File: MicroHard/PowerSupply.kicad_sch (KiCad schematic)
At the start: 40 parts, among them J1 USB_B_Micro, U1 TPS54325, U2 TPS54294

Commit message: VGA and Display layout
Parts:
- R8: value 68 -> 330
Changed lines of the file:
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@@
 			)
 		)
-		(property "Value" "68"
+		(property "Value" "330"
 			(at 240.284 133.604 0)
 			(effects

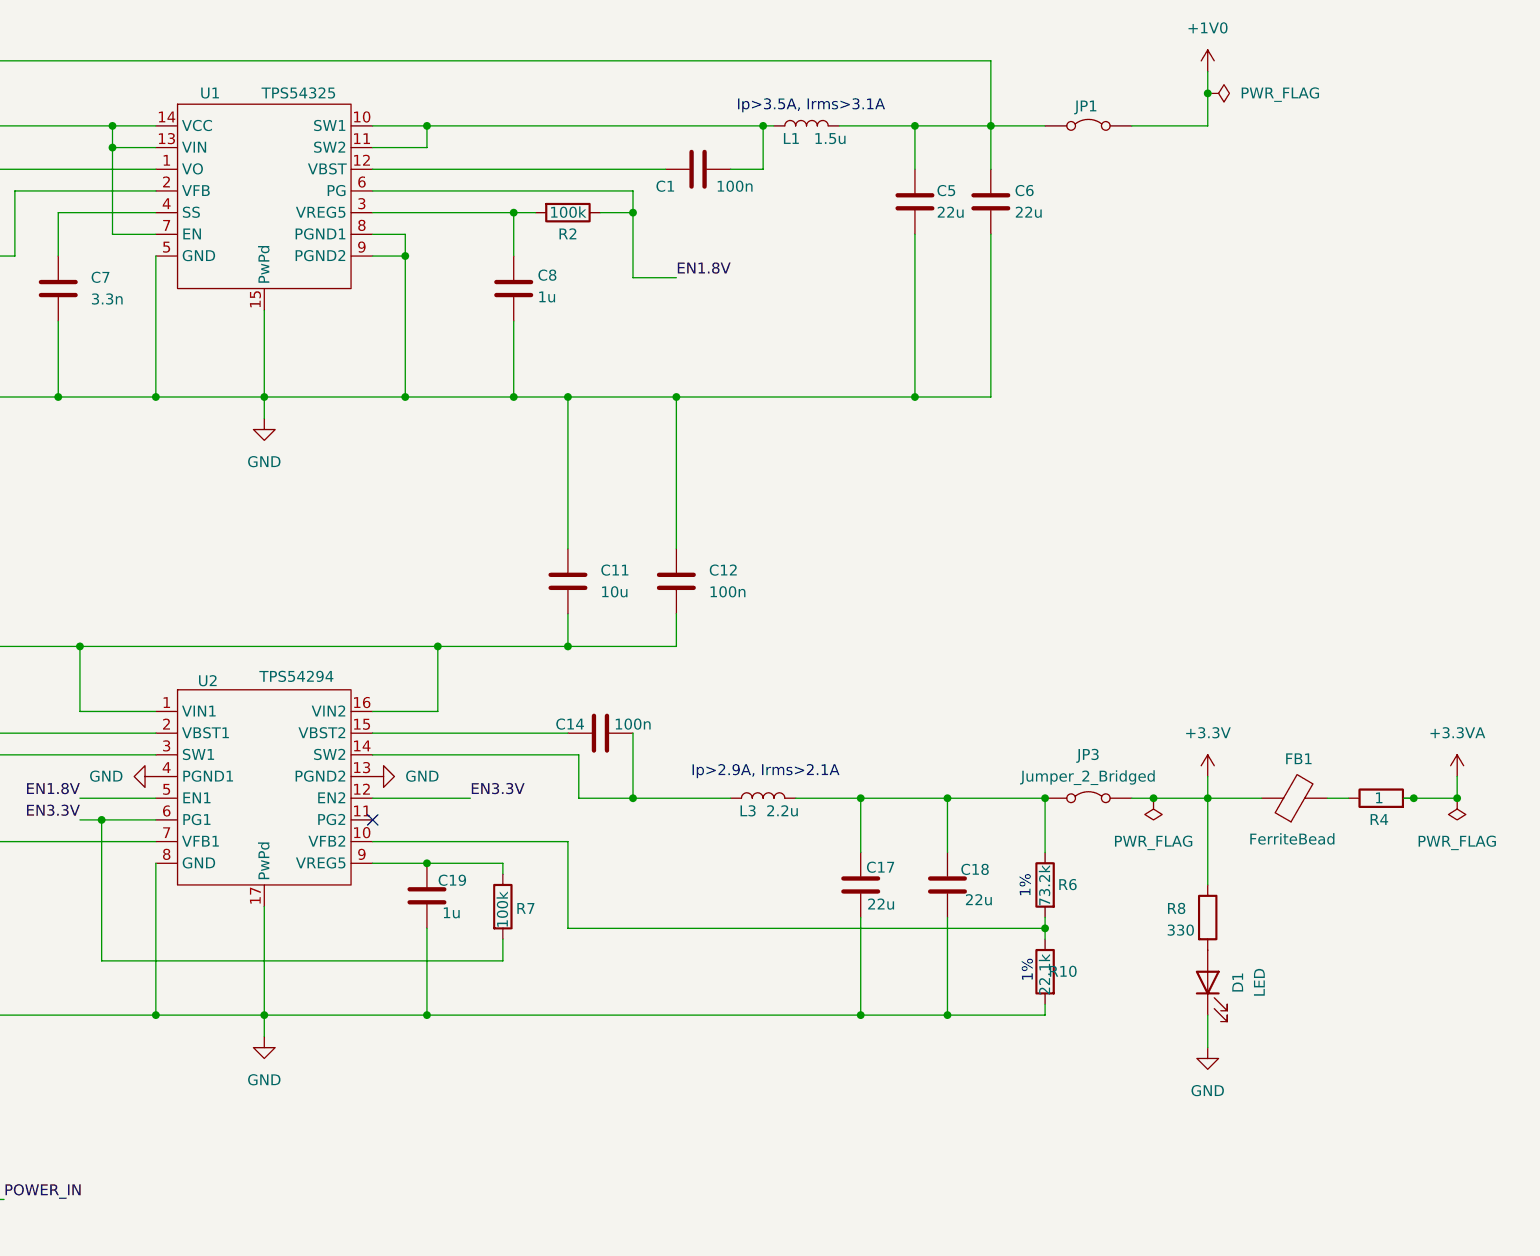
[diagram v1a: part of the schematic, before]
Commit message: Power supply layout
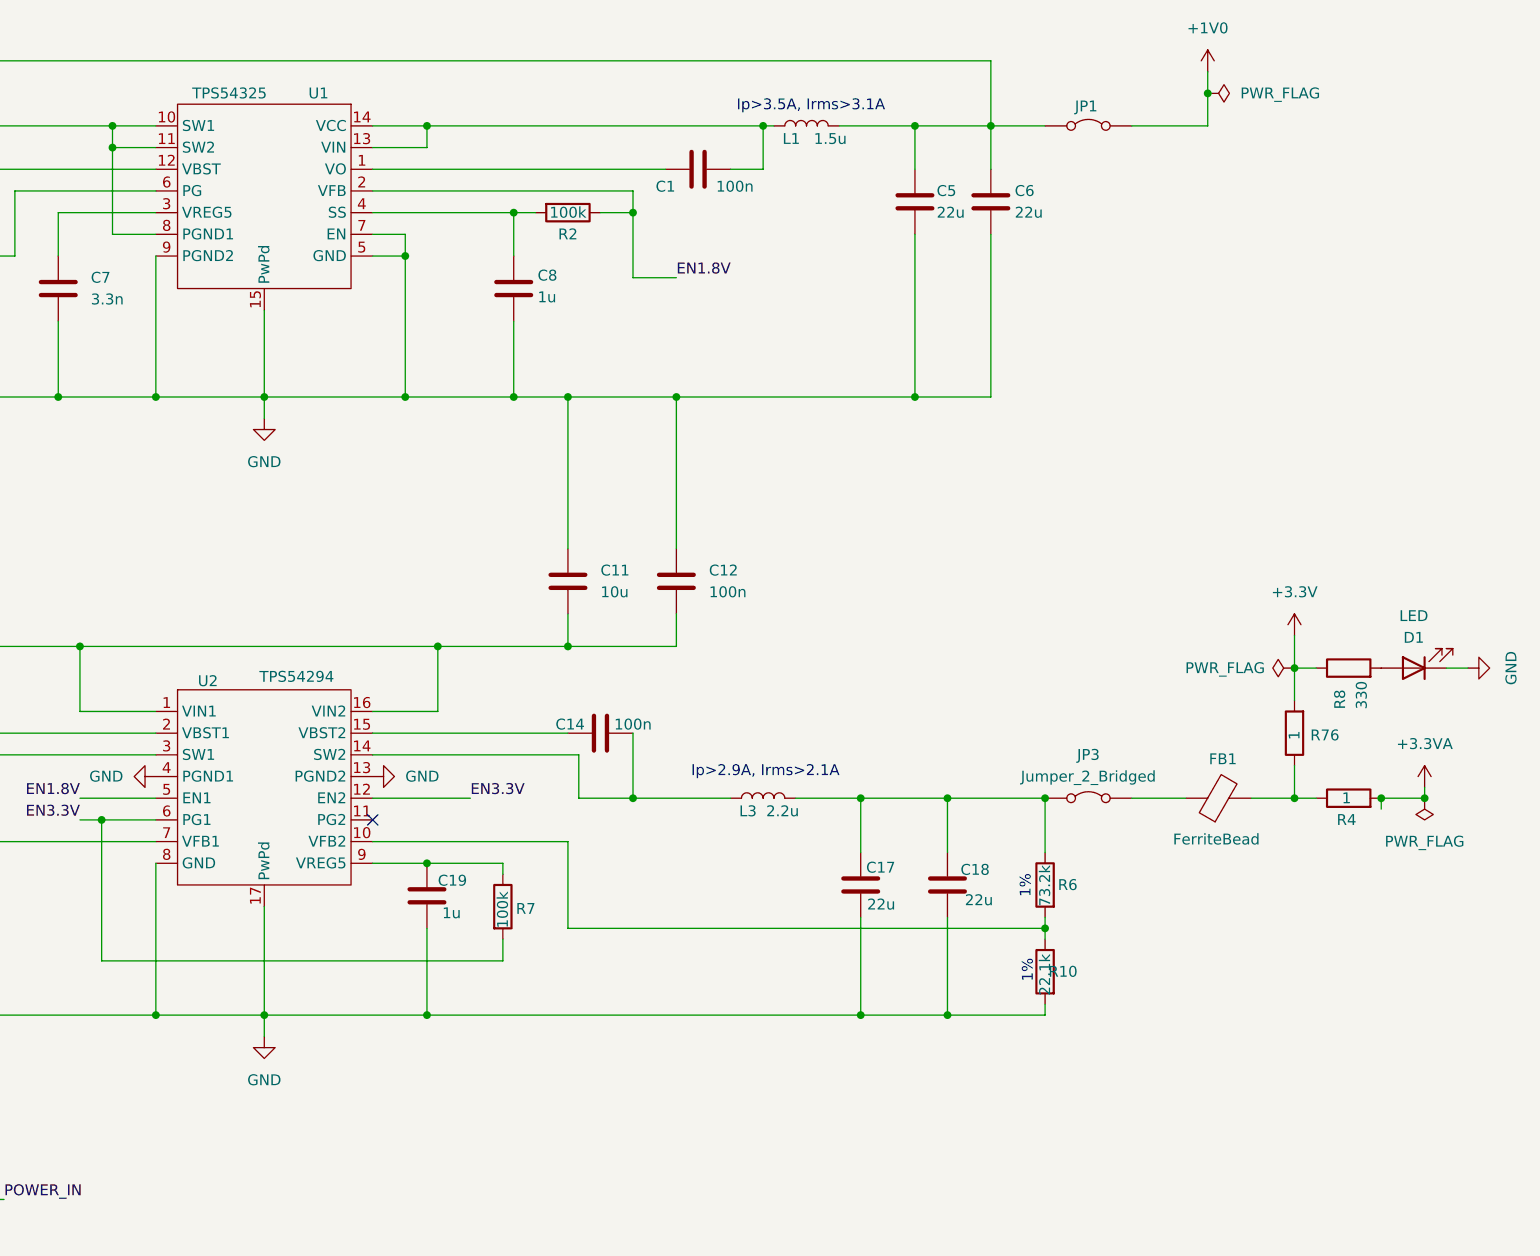
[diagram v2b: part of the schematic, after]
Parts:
- added R76: 1, Resistor_SMD:R_1206_3216Metric_Pad1.30x1.75mm_HandSolder, symbol Device:R
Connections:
- net +3.3V: now also R76.2; no longer FB1.1, JP3.2 (B)
- net EN1.8V: now also U1.2 (VFB); no longer U1.6 (PG)
- net GND: now also U1.7 (EN); no longer U1.8 (PGND1)
- net POWER_IN: now also U1.10 (SW1), U1.11 (SW2), U1.8 (PGND1); no longer U1.13 (VIN), U1.14 (VCC), U1.7 (EN)
- net at C5.1, C6.1, JP1.1 (A)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: now also U1.12 (VBST); no longer U1.1 (VO)
- net at FB1.2, R4.1: now also R76.1
- net at C7.1: now also U1.3 (VREG5); no longer U1.4 (SS)
- net at C8.1, R2.2: now also U1.4 (SS); no longer U1.3 (VREG5)
- net at C1.1, L1.1: now also U1.13 (VIN), U1.14 (VCC); no longer U1.10 (SW1), U1.11 (SW2)
- net at C1.2: now also U1.1 (VO); no longer U1.12 (VBST)
- net at R1.2, R3.1: now also U1.6 (PG); no longer U1.2 (VFB)
- new net: FB1.1, JP3.2 (B)
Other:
- moved on the sheet: D1, FB1, R4, R8

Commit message: Change inductor footprint
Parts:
- L1, L2, L3: footprint Inductor_SMD:L_1206_3216Metric_Pad1.42x1.75mm_HandSolder -> 74438357022 Wuerth Inductor:IND_8357022_WRE
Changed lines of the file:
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@@
 			)
 		)
-		(property "Footprint" "Inductor_SMD:L_1206_3216Metric_Pad1.42x1.75mm_HandSolder"
+		(property "Footprint" "74438357022 Wuerth Inductor:IND_8357022_WRE"
 			(at 193.04 118.11 0)
 			(effects
@@
 			)
 		)
-		(property "Footprint" "Inductor_SMD:L_1206_3216Metric_Pad1.42x1.75mm_HandSolder"
+		(property "Footprint" "74438357022 Wuerth Inductor:IND_8357022_WRE"
 			(at 76.2 118.11 0)
 			(effects
@@
 			)
 		)
-		(property "Footprint" "Inductor_SMD:L_1206_3216Metric_Pad1.42x1.75mm_HandSolder"
+		(property "Footprint" "74438357022 Wuerth Inductor:IND_8357022_WRE"
 			(at 198.12 39.37 0)
 			(effects
